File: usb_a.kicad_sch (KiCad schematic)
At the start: 3 parts, among them J2 U-A-39SS-Y-1, U2 TPD2EUSB30, U3 TPD4EUSB30

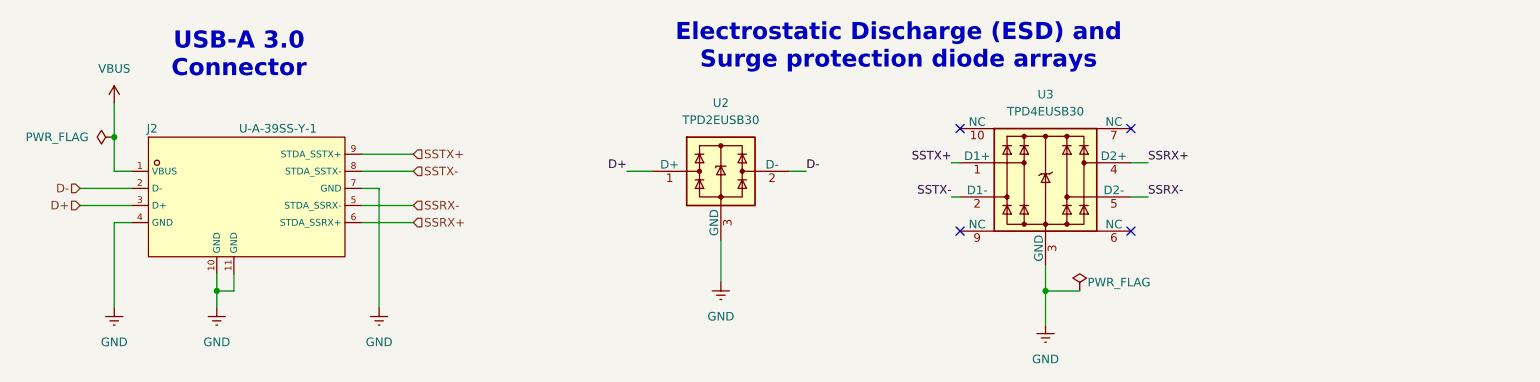
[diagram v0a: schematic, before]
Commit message: Routing Complete (DRC Checker Errors needs fixing)
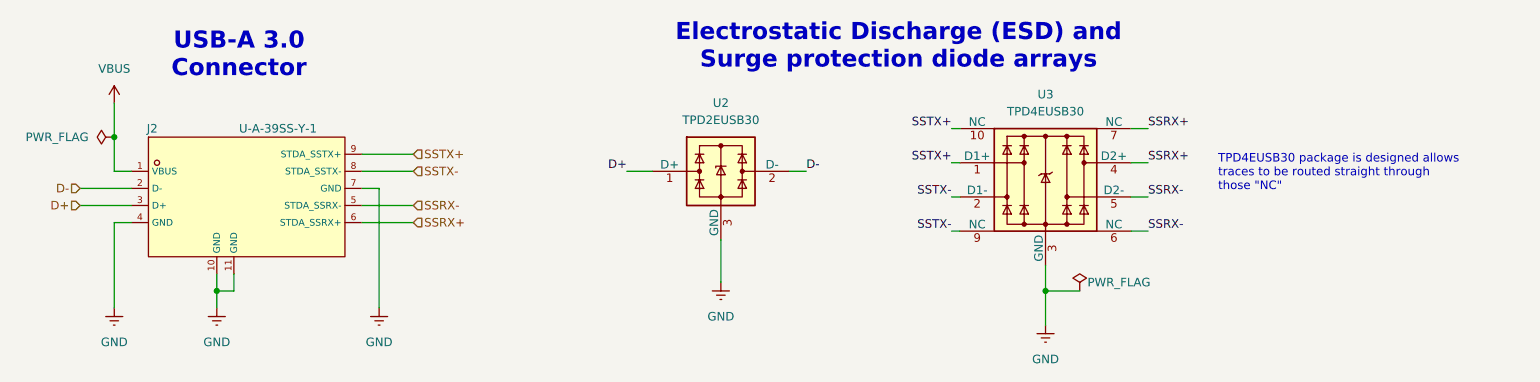
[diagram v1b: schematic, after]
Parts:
- J2: footprint footprint:USB-3.0-A_U-A-39SS-Y-1 -> Interface_USB:USB-3.0-A_U-A-39SS-Y-1
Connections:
- net SSRX+: now also U3.7 (NC)
- net SSRX-: now also U3.6 (NC)
- net SSTX+: now also U3.10 (NC)
- net SSTX-: now also U3.9 (NC)
- no-connect marks 4 -> 0
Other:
- note added: "TPD4EUSB30 package is designed allows traces to be routed straight through those "NC""
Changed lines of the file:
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@@
+		)
+	)
+	(text "TPD4EUSB30 package is designed allows \ntraces to be routed straight through \nthose \"NC\"\n"
+		(exclude_from_sim no)
+		(at 221.234 94.234 0)
+		(effects
+			(font
+				(size 1.27 1.27)
+			)
+			(justify left)
 		)
 	)
@@
 		(color 0 0 0 0)
 	)
-	(no_connect
-		(at 182.88 87.63)
-	)
-	(no_connect
-		(at 182.88 102.87)
-	)
-	(no_connect
-		(at 208.28 102.87)
-	)
-	(no_connect
-		(at 208.28 87.63)
+	(wire
+		(pts
+			(xy 181.61 87.63) (xy 182.88 87.63)
+		)
+		(stroke
+			(width 0)
+			(type default)
+		)
 	)
 	(wire
@@
 	(wire
 		(pts
+			(xy 208.28 87.63) (xy 210.82 87.63)
+		)
+		(stroke
+			(width 0)
+			(type default)
+		)
+	)
+	(wire
+		(pts
+			(xy 181.61 102.87) (xy 182.88 102.87)
+		)
+		(stroke
+			(width 0)
+			(type default)
+		)
+	)
+	(wire
+		(pts
 			(xy 93.98 101.6) (xy 101.6 101.6)
 		)
@@
 		(pts
 			(xy 195.58 111.76) (xy 200.66 111.76)
+		)
+		(stroke
+			(width 0)
+			(type default)
+		)
+	)
+	(wire
+		(pts
+			(xy 208.28 102.87) (xy 210.82 102.87)
 		)
 		(stroke
@@
 		)
 	)
+	(label "SSRX+"
+		(at 210.82 87.63 0)
+		(effects
+			(font
+				(size 1.27 1.27)
+			)
+			(justify left bottom)
+		)
+	)
 	(label "D-"
 		(at 160.02 93.98 0)
@@
 			)
 			(justify left bottom)
+		)
+	)
+	(label "SSTX-"
+		(at 181.61 102.87 180)
+		(effects
+			(font
+				(size 1.27 1.27)
+			)
+			(justify right bottom)
+		)
+	)
+	(label "SSRX-"
+		(at 210.82 102.87 0)
+		(effects
+			(font
+				(size 1.27 1.27)
+			)
+			(justify left bottom)
+		)
+	)
+	(label "SSTX+"
+		(at 181.61 87.63 180)
+		(effects
+			(font
+				(size 1.27 1.27)
+			)
+			(justify right bottom)
 		)
 	)
@@
 			)
 		)
-		(property "Footprint" "footprint:USB-3.0-A_U-A-39SS-Y-1"
+		(property "Footprint" "Interface_USB:USB-3.0-A_U-A-39SS-Y-1"
 			(at 77.47 107.95 0)
 			(hide yes)

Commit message: DRC Errors Fixed, BOM Cleaned up and Generated, Gerber Generated
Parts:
- J2: Store Page (none) -> https://item.szlcsc.com/550973.html; Unit Price (none) -> 0.3147
- U2: LCSC (none) -> C97502; Store Page (none) -> https://www.lcsc.com/product-detail/C97502.html; Unit Price (none) -> 0.5436
- U3: LCSC (none) -> C90627; Store Page (none) -> https://www.lcsc.com/product-detail/C90627.html; Unit Price (none) -> 0.4568
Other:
- company: (none) -> UWaterloo Reality Labs
- title: (none) -> USB-3.0 Bridging Board Type-A Interface
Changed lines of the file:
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@@
 	(generator_version "10.0")
 	(paper "A4")
+	(title_block
+		(title "USB-3.0 Bridging Board Type-A Interface")
+		(date "2026-04-16")
+		(rev "R1")
+		(company "UWaterloo Reality Labs")
+		(comment 4 "Authors: Brandon, Marcus, Dinh")
+	)
 	(text "USB-A 3.0\nConnector"
 		(exclude_from_sim no)
@@
 			)
 		)
+		(property "Store Page" "https://www.lcsc.com/product-detail/C97502.html"
+			(at 147.32 93.98 0)
+			(hide yes)
+			(show_name no)
+			(do_not_autoplace no)
+			(effects
+				(font
+					(size 1.27 1.27)
+				)
+			)
+		)
+		(property "LCSC" "C97502"
+			(at 147.32 93.98 0)
+			(hide yes)
+			(show_name no)
+			(do_not_autoplace no)
+			(effects
+				(font
+					(size 1.27 1.27)
+				)
+			)
+		)
+		(property "Unit Price" "0.5436"
+			(at 147.32 93.98 0)
+			(hide yes)
+			(show_name no)
+			(do_not_autoplace no)
+			(effects
+				(font
+					(size 1.27 1.27)
+				)
+			)
+		)
 		(pin "1"
 		)
@@
 			)
 		)
+		(property "Store Page" "https://www.lcsc.com/product-detail/C90627.html"
+			(at 195.58 95.25 0)
+			(hide yes)
+			(show_name no)
+			(do_not_autoplace no)
+			(effects
+				(font
+					(size 1.27 1.27)
+				)
+			)
+		)
+		(property "LCSC" "C90627"
+			(at 195.58 95.25 0)
+			(hide yes)
+			(show_name no)
+			(do_not_autoplace no)
+			(effects
+				(font
+					(size 1.27 1.27)
+				)
+			)
+		)
+		(property "Unit Price" "0.4568"
+			(at 195.58 95.25 0)
+			(hide yes)
+			(show_name no)
+			(do_not_autoplace no)
+			(effects
+				(font
+					(size 1.27 1.27)
+				)
+			)
+		)
 		(pin "6"
 		)
@@
 			)
 		)
-		(property "Datasheet" "https://item.szlcsc.com/550973.html"
+		(property "Datasheet" ""
 			(at 75.184 97.663 0)
 			(hide yes)
@@
 		)
 		(property "LCSC" "C530639"
+			(at 77.47 97.79 0)
+			(hide yes)
+			(show_name no)
+			(do_not_autoplace no)
+			(effects
+				(font
+					(size 1.27 1.27)
+				)
+			)
+		)
+		(property "Store Page" "https://item.szlcsc.com/550973.html"
+			(at 77.47 97.79 0)
+			(hide yes)
+			(show_name no)
+			(do_not_autoplace no)
+			(effects
+				(font
+					(size 1.27 1.27)
+				)
+			)
+		)
+		(property "Unit Price" "0.3147"
 			(at 77.47 97.79 0)
 			(hide yes)
@@
 		)
 		(property "Value" "PWR_FLAG"
-			(at 206.502 110.49 0)
-			(show_name no)
-			(do_not_autoplace no)
+			(at 206.756 110.49 0)
+			(show_name no)
+			(do_not_autoplace no)
